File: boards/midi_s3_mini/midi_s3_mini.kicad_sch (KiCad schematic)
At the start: 64 parts, among them J1 OneButtonA_TX, J10 JOG, J2 OneButtonA_RX, J3 OneButtonB_RX, J4 OneButtonB_TX, J5 UART_PI, J6 TRACK_ENC, J7 LOOP, J8 PLAY_CUE, J9 TEMPO, U1 LOLIN_S3_Mini

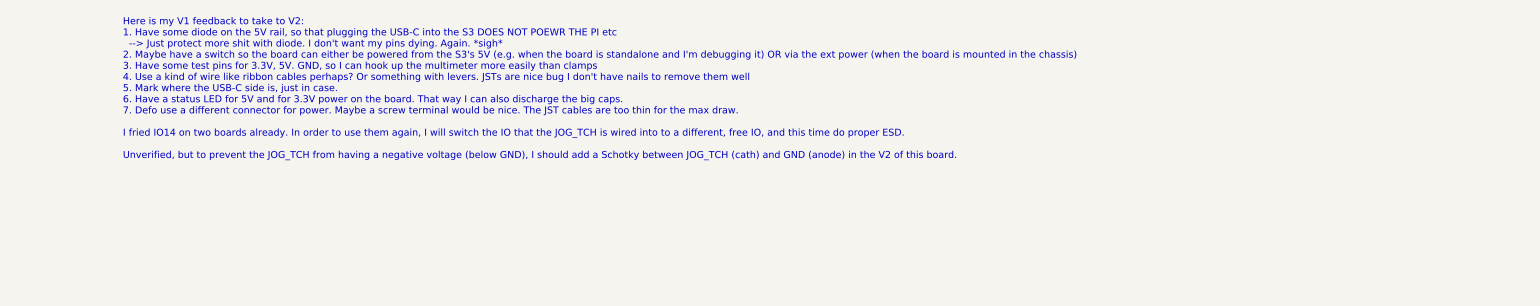
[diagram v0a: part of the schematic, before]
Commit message: Finish PCB silkscreen and final placement
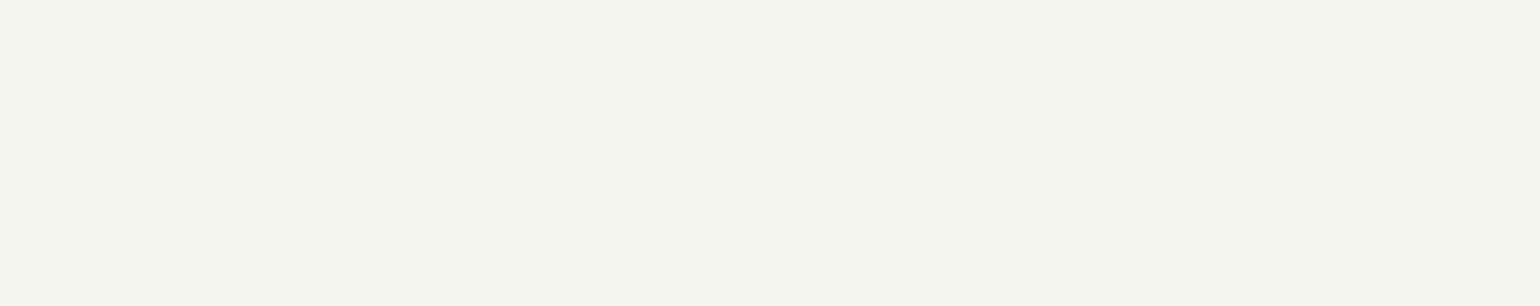
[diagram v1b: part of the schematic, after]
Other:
- note removed: "Here is my V1 feedback to take to V2: 1. Have some diode on the 5V rail, so that plugging the USB-C into the S3 DOES NOT POEWR THE PI etc --> Just protect more shit with diode. I don't want my pins dying. Again. *sigh* 2. Maybe have a switch so the board can either be powered from the S3's 5V (e.g. when the board is standalone and I'm debugging it) OR via the ext power (when the board is mounted 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"
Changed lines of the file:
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@@
-		)
-	)
-	(text "Here is my V1 feedback to take to V2:\n1. Have some diode on the 5V rail, so that plugging the USB-C into the S3 DOES NOT POEWR THE PI etc\n  --> Just protect more shit with diode. I don't want my pins dying. Again. *sigh*\n2. Maybe have a switch so the board can either be powered from the S3's 5V (e.g. when the board is standalone and I'm debugging it) OR via the ext power (when the board is mounted in the chassis)\n3. Have some test pins for 3.3V, 5V. GND, so I can hook up the multimeter more easily than clamps\n4. Use a kind of wire like ribbon cables perhaps? Or something with levers. JSTs are nice bug I don't have nails to remove them well\n5. Mark where the USB-C side is, just in case.\n6. Have a status LED for 5V and for 3.3V power on the board. That way I can also discharge the big caps.\n7. Defo use a different connector for power. Maybe a screw terminal would be nice. The JST cables are too thin for the max draw.\n\nI fried IO14 on two boards already. In order to use them again, I will switch the IO that the JOG_TCH is wired into to a different, free IO, and this time do proper ESD.\n\nUnverified, but to prevent the JOG_TCH from having a negative voltage (below GND), I should add a Schotky between JOG_TCH (cath) and GND (anode) in the V2 of this board."
-		(exclude_from_sim no)
-		(at 24.892 -5.842 0)
-		(effects
-			(font
-				(size 1 1)
-			)
-			(justify left)
 		)
 	)

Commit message: Finally fabbed v2
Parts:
- J1: value OneButtonA_TX -> 1BTN_A_TX; now left out of the parts list
- J10, J5, J6, J7, J8, J9, TP1, U1: now left out of the parts list
- J2: value OneButtonA_RX -> 1BTN_A_RX; now left out of the parts list
- J3: value OneButtonB_RX -> 1BTN_B_RX; now left out of the parts list
- J4: value OneButtonB_TX -> 1BTN_B_TX; now left out of the parts list
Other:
- note added: "Somehow 10k was out of stock. Went with 22k pullup. No noticeable impact in practice."
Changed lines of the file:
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@@
 		)
 	)
+	(text "Somehow 10k was out of stock.\nWent with 22k pullup. \nNo noticeable impact in practice."
+		(exclude_from_sim no)
+		(at 271.526 212.344 0)
+		(effects
+			(font
+				(size 1.27 1.27)
+			)
+			(justify left)
+		)
+	)
 	(junction
 		(at 43.18 248.92)
@@
 		(body_style 1)
 		(exclude_from_sim no)
-		(in_bom yes)
+		(in_bom no)
 		(on_board yes)
-		(in_pos_files yes)
+		(in_pos_files no)
 		(dnp no)
 		(fields_autoplaced yes)
@@
 		(in_bom no)
 		(on_board yes)
-		(in_pos_files yes)
+		(in_pos_files no)
 		(dnp no)
 		(fields_autoplaced yes)
@@
 		(body_style 1)
 		(exclude_from_sim no)
-		(in_bom yes)
+		(in_bom no)
 		(on_board yes)
-		(in_pos_files yes)
+		(in_pos_files no)
 		(dnp no)
 		(fields_autoplaced yes)
@@
 			)
 		)
-		(property "Value" "OneButtonA_RX"
+		(property "Value" "1BTN_A_RX"
 			(at 304.8 53.3399 0)
 			(show_name no)
@@
 		(body_style 1)
 		(exclude_from_sim no)
-		(in_bom yes)
+		(in_bom no)
 		(on_board yes)
-		(in_pos_files yes)
+		(in_pos_files no)
 		(dnp no)
 		(fields_autoplaced yes)
@@
 		(in_bom no)
 		(on_board yes)
-		(in_pos_files yes)
+		(in_pos_files no)
 		(dnp no)
 		(fields_autoplaced yes)
@@
 		(in_bom no)
 		(on_board yes)
-		(in_pos_files yes)
+		(in_pos_files no)
 		(dnp no)
 		(fields_autoplaced yes)
@@
 		(in_bom no)
 		(on_board yes)
-		(in_pos_files yes)
+		(in_pos_files no)
 		(dnp no)
 		(fields_autoplaced yes)
@@
 		(in_bom no)
 		(on_board yes)
-		(in_pos_files yes)
+		(in_pos_files no)
 		(dnp no)
 		(fields_autoplaced yes)
@@
 		(body_style 1)
 		(exclude_from_sim no)
-		(in_bom yes)
+		(in_bom no)
 		(on_board yes)
-		(in_pos_files yes)
+		(in_pos_files no)
 		(dnp no)
 		(fields_autoplaced yes)
@@
 		(body_style 1)
 		(exclude_from_sim no)
-		(in_bom yes)
+		(in_bom no)
 		(on_board yes)
-		(in_pos_files yes)
+		(in_pos_files no)
 		(dnp no)
 		(fields_autoplaced yes)
@@
 		(body_style 1)
 		(exclude_from_sim no)
-		(in_bom yes)
+		(in_bom no)
 		(on_board yes)
-		(in_pos_files yes)
+		(in_pos_files no)
 		(dnp no)
 		(fields_autoplaced yes)
@@
 		(in_bom no)
 		(on_board yes)
-		(in_pos_files yes)
+		(in_pos_files no)
 		(dnp no)
 		(fields_autoplaced yes)
@@
 		(body_style 1)
 		(exclude_from_sim no)
-		(in_bom yes)
+		(in_bom no)
 		(on_board yes)
-		(in_pos_files yes)
+		(in_pos_files no)
 		(dnp no)
 		(fields_autoplaced yes)
@@
 			)
 		)
-		(property "Value" "OneButtonB_RX"
+		(property "Value" "1BTN_B_RX"
 			(at 308.61 88.8999 0)
 			(show_name no)
@@
 		(body_style 1)
 		(exclude_from_sim no)
-		(in_bom yes)
+		(in_bom no)
 		(on_board yes)
-		(in_pos_files yes)
+		(in_pos_files no)
 		(dnp no)
 		(fields_autoplaced yes)
@@
 			)
 		)
-		(property "Value" "OneButtonB_TX"
+		(property "Value" "1BTN_B_TX"
 			(at 330.2 100.3299 0)
 			(show_name no)
@@
 		(in_bom no)
 		(on_board yes)
-		(in_pos_files yes)
+		(in_pos_files no)
 		(dnp no)
 		(fields_autoplaced yes)
@@
 		(body_style 1)
 		(exclude_from_sim no)
-		(in_bom yes)
+		(in_bom no)
 		(on_board yes)
-		(in_pos_files yes)
+		(in_pos_files no)
 		(dnp no)
 		(fields_autoplaced yes)
@@
 			)
 		)
-		(property "Value" "OneButtonA_TX"
+		(property "Value" "1BTN_A_TX"
 			(at 335.28 52.0699 0)
 			(show_name no)
@@
 		(body_style 1)
 		(exclude_from_sim no)
-		(in_bom yes)
+		(in_bom no)
 		(on_board yes)
-		(in_pos_files yes)
+		(in_pos_files no)
 		(dnp no)
 		(fields_autoplaced yes)
@@
 		(body_style 1)
 		(exclude_from_sim no)
-		(in_bom yes)
+		(in_bom no)
 		(on_board yes)
-		(in_pos_files yes)
+		(in_pos_files no)
 		(dnp no)
 		(fields_autoplaced yes)
@@
 		(body_style 1)
 		(exclude_from_sim no)
-		(in_bom yes)
+		(in_bom no)
 		(on_board yes)
-		(in_pos_files yes)
+		(in_pos_files no)
 		(dnp no)
 		(fields_autoplaced yes)
